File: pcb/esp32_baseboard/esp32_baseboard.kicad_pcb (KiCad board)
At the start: 2 copper layers, 150 x 130 mm, 77 parts, among them J1 24V_IN, J14 BUP_U, J15 FIBER, U1 STM32G030C8T6, U2 MP1584EN, U3 TMC1, U4 TMC2, U44 PC817, U45 PC817, U46 PC817, U5 CH340C, U6 AMS1117-3.3, U7 TM1637, Y1 12MHz

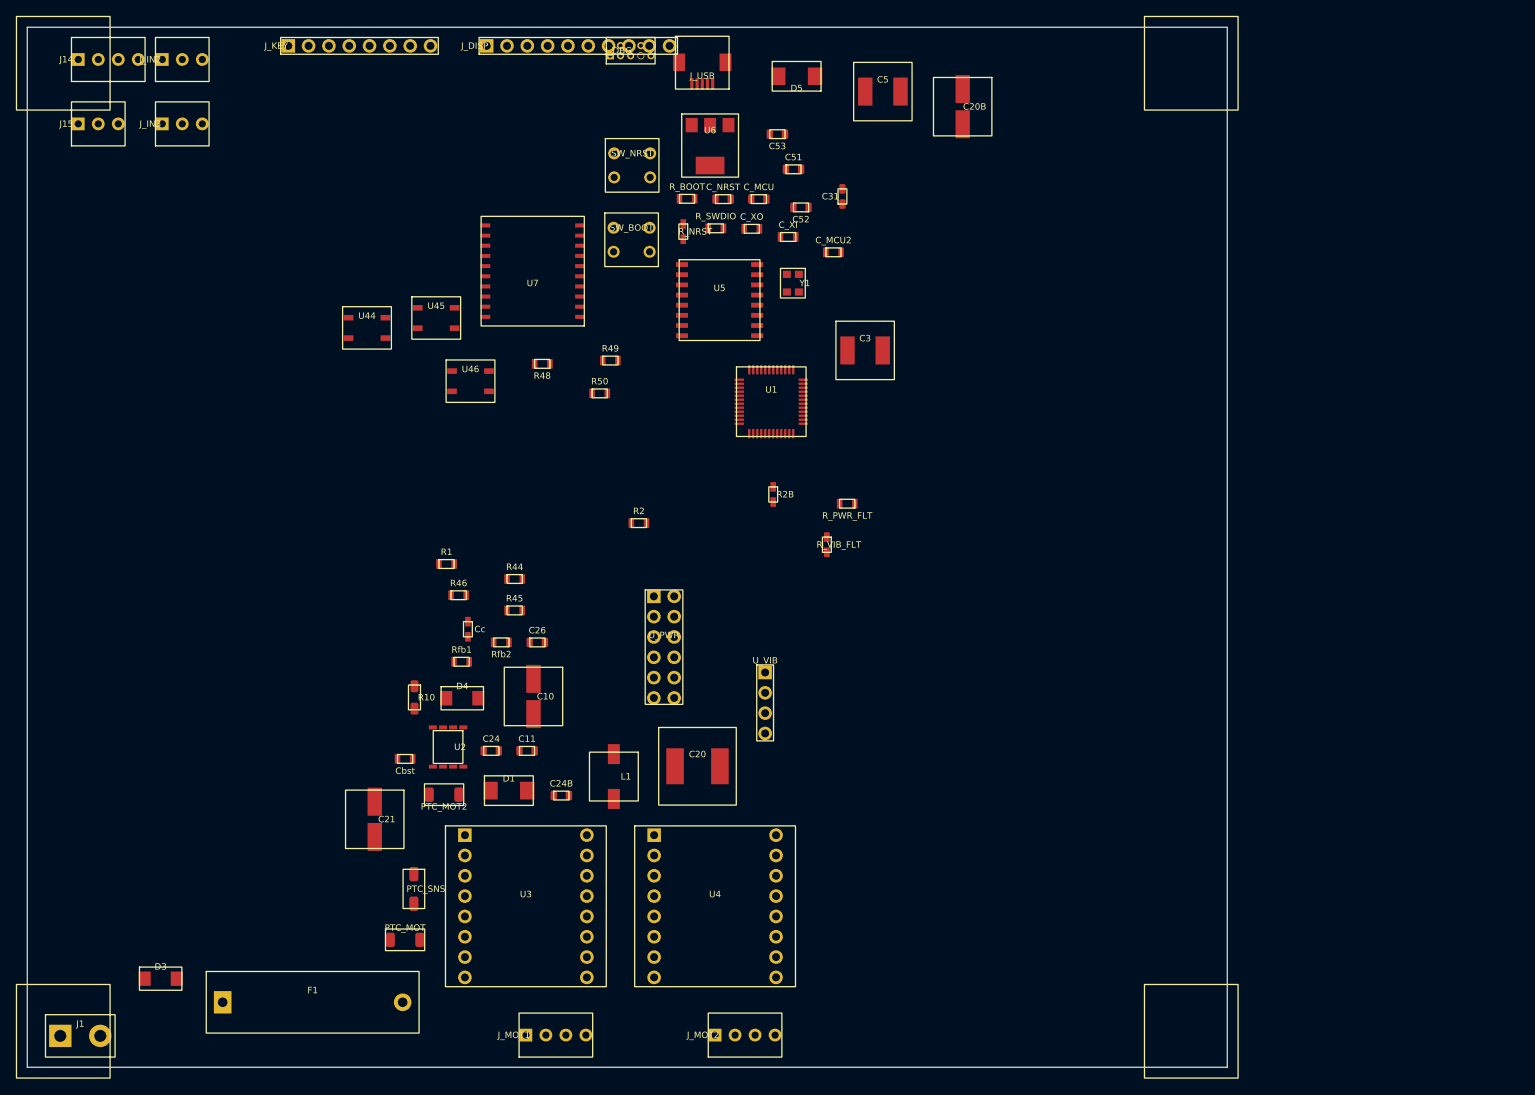
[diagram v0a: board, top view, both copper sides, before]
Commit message: Cập nhật carrier STM32: giắc N/S, USB+BOOT/RESET, courtyard ≥2.5mm.
Xóa pcb/esp32_soldered/.history và ignore thư mục .history.

Co-authored-by: Cursor <cursoragent@cursor.com>
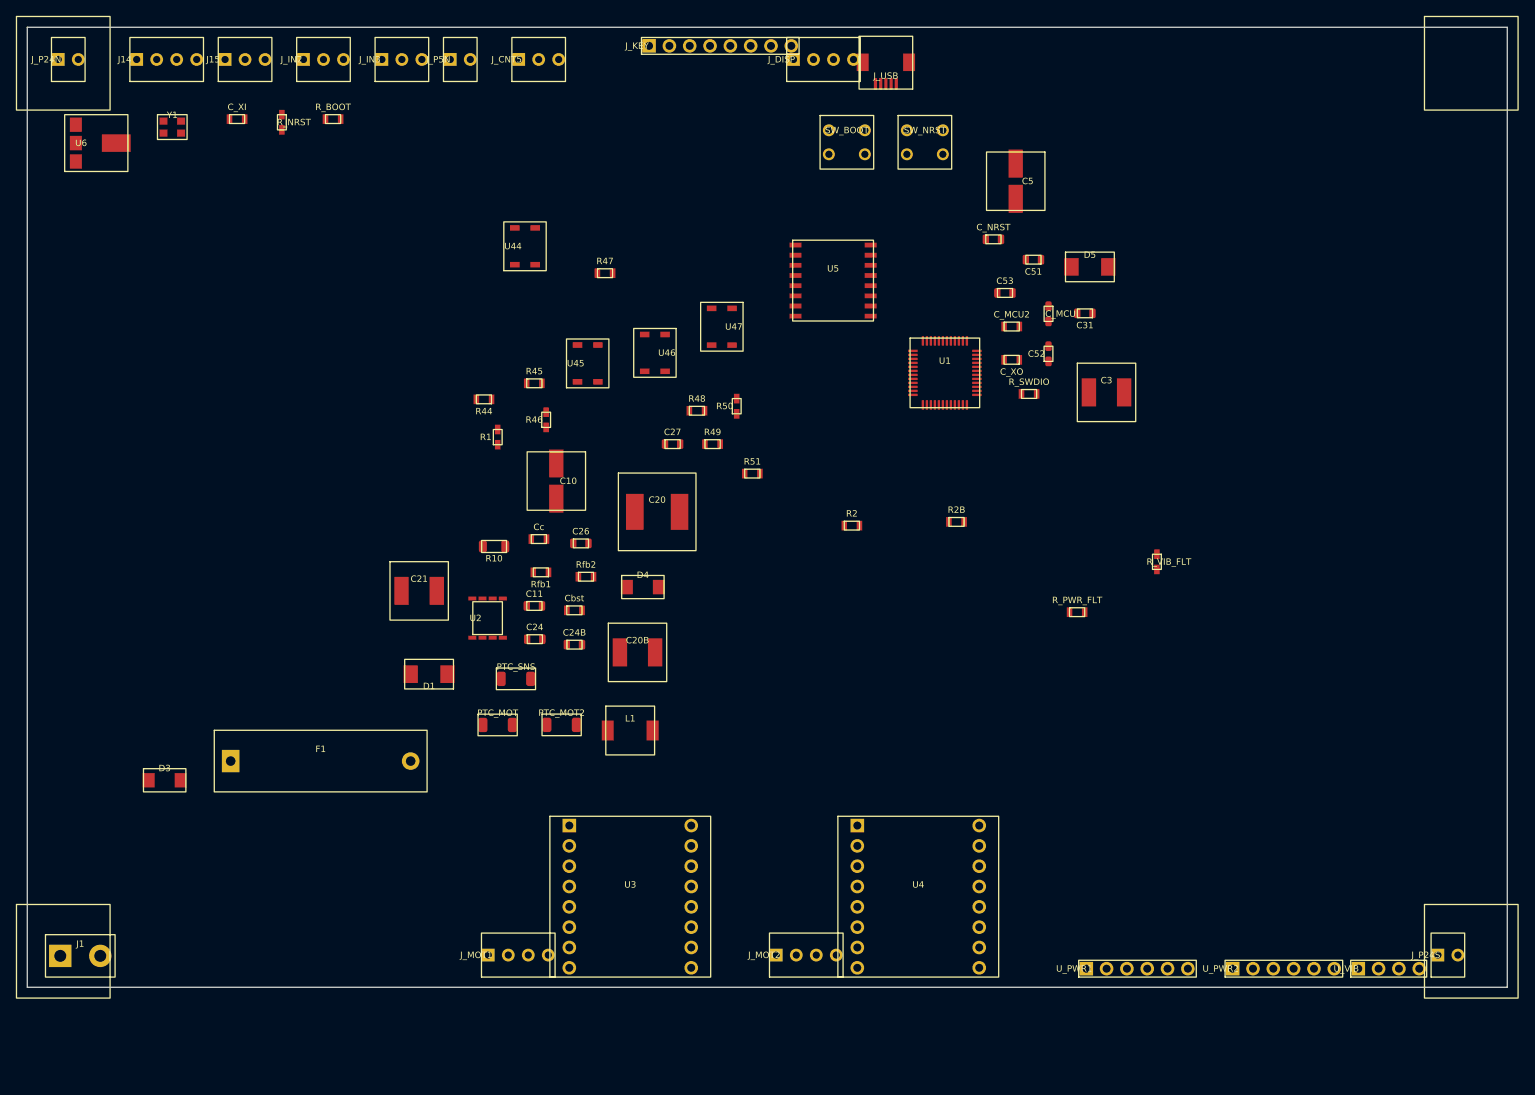
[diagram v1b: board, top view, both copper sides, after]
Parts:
- removed J_DBG: CortexDbg, ESP32_Carrier:Cortex_Debug_10
- removed the J_DISP at (107.4, 52.3)
- removed U7: TM1637, ESP32_Carrier:TM1637_SOP20
- removed U_PWR: PWR_MOD, ESP32_Carrier:PowerMod_2CH_Sock
- added C27: 100n, ESP32_Carrier:C_0805_100n, F.Cu at (130.7, 102.1)
- added J_CNT5: CNT5V, ESP32_Carrier:JST_XH_03_Socket, F.Cu at (111.4, 54.0)
- added J_DISP: TM1637_MOD, ESP32_Carrier:Disp_XH_04_Socket, F.Cu at (145.8, 54.0)
- added J_P24N: P24_N, ESP32_Carrier:JST_XH_02_Socket, F.Cu at (53.9, 54.0)
- added J_P24S: P24_S, ESP32_Carrier:JST_XH_02_Socket, F.Cu at (226.3, 166.0)
- added J_P5N: P5_N, ESP32_Carrier:JST_XH_02_Socket, F.Cu at (102.9, 54.0)
- added R47: 1k, ESP32_Carrier:R_0805_1k, F.Cu at (122.2, 80.7)
- added R51: 10k, ESP32_Carrier:R_0805_10k, F.Cu at (140.6, 105.8)
- added U47: PC817, ESP32_Carrier:PC817_SOP4, F.Cu at (136.8, 87.4)
- added U_PWR1: FET1, ESP32_Carrier:PowerMod_1CH_Sock, F.Cu at (182.4, 167.7)
- added U_PWR2: FET2, ESP32_Carrier:PowerMod_1CH_Sock, F.Cu at (200.7, 167.7)
- moved U_VIB 82.9 mm to (216.4, 167.7), turned to 90 degrees
- moved Y1 80.0 mm to (68.1, 62.5), turned to 0 degrees
- moved C20B 79.4 mm to (126.3, 128.1), turned to 0 degrees
- moved U6 77.1 mm to (58.2, 64.5), turned to 90 degrees
- moved C_XI 70.4 mm to (76.2, 61.5)
- moved R_NRST 52.0 mm to (81.8, 61.9)
- moved R_BOOT 45.4 mm to (88.2, 61.5)
- moved J_KEY 45.1 mm to (127.7, 52.3)
- moved R_SWDIO 44.3 mm to (175.2, 95.8)
- moved D5 43.7 mm to (182.8, 80.0), turned to 0 degrees
- moved R_VIB_FLT 41.3 mm to (191.2, 116.8)
- moved C_MCU 38.9 mm to (177.7, 85.8), turned to 270 degrees
- moved SW_NRST 36.7 mm to (162.2, 64.4)
- moved H4 36.4 mm to (230.5, 165.5)
- moved C_XO 36.4 mm to (173.1, 91.6), turned to 180 degrees
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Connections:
- U1 pad 39: (no net) -> /CNT5
- U1 pad 42: /SWO -> (no net)
- U1 pad 44: /PWR_EN -> /PWR_EN1
- U1 pad 45: /PWR_DIR -> /PWR_EN2
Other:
- board size 150 x 130 mm -> 185 x 120 mm
- board text added: "185x120 DIN | field jacks N/S only | W/E=rail"
- board text added: "N: SNS/HMI/USB | S: J1 MOT1 U3 MOT2 U4 PWR1 PWR2 VIB P24"
- board text removed: "150x130 DIN | field jacks N/S only | W/E=rail"
- board text removed: "N: SNS/KEY/DISP | S: J1 MOT USB DBG | no side jacks"
